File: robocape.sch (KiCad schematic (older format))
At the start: 5 parts

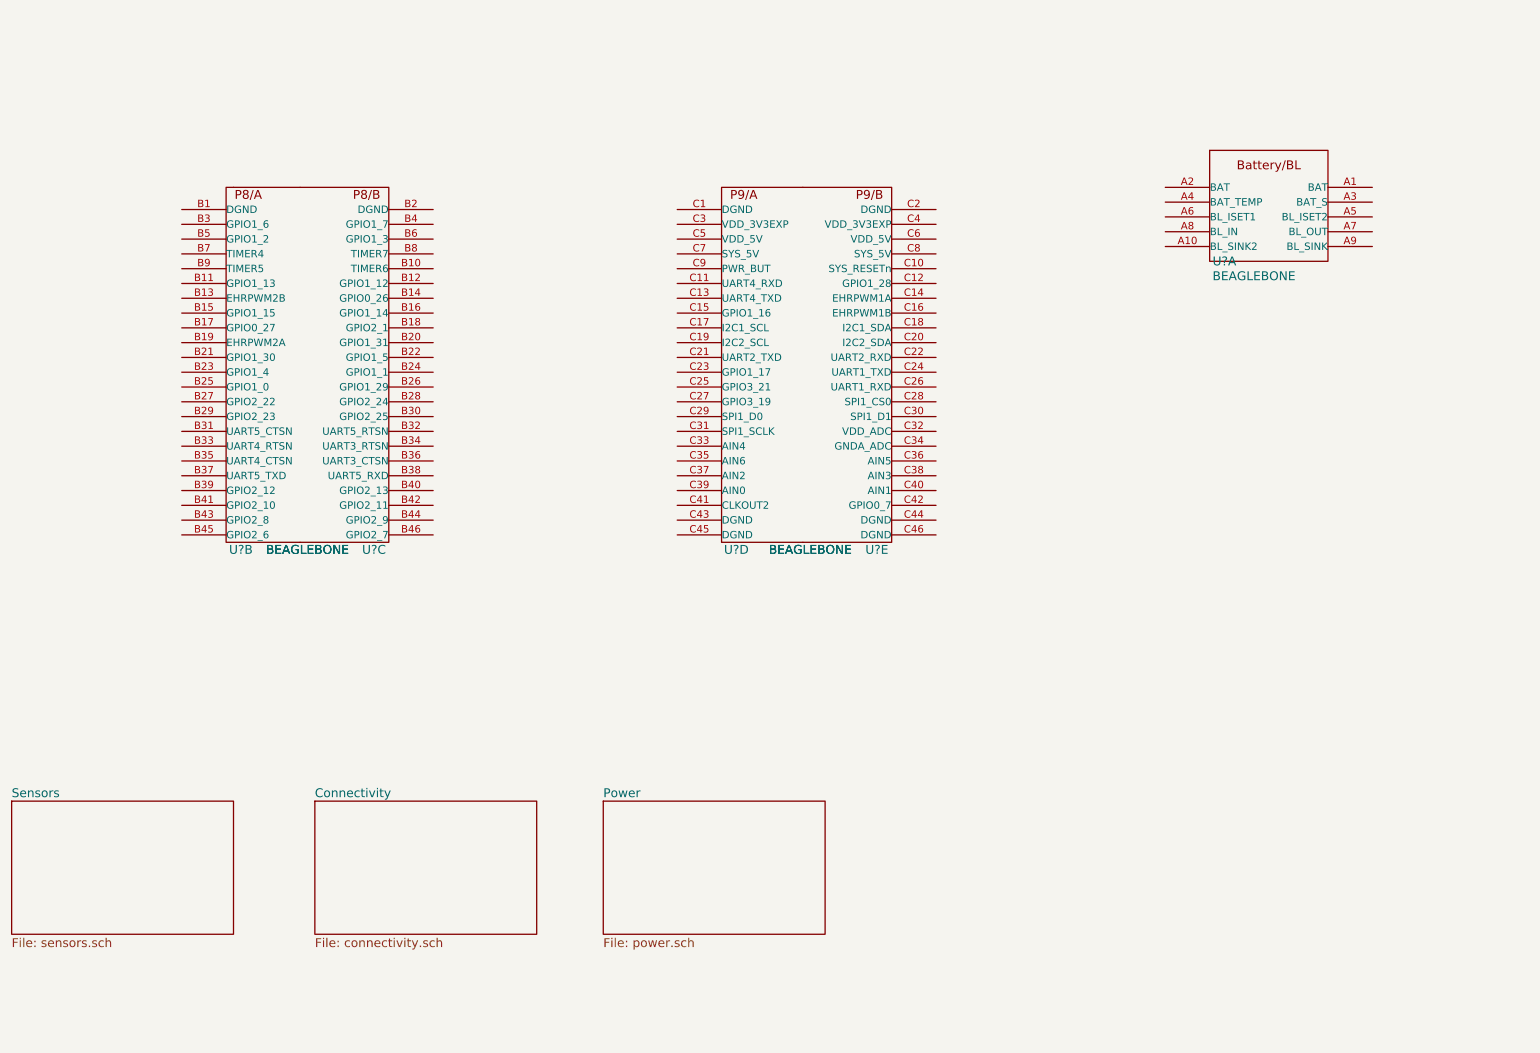
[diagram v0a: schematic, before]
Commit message: Schematic: EEPROM + IMU
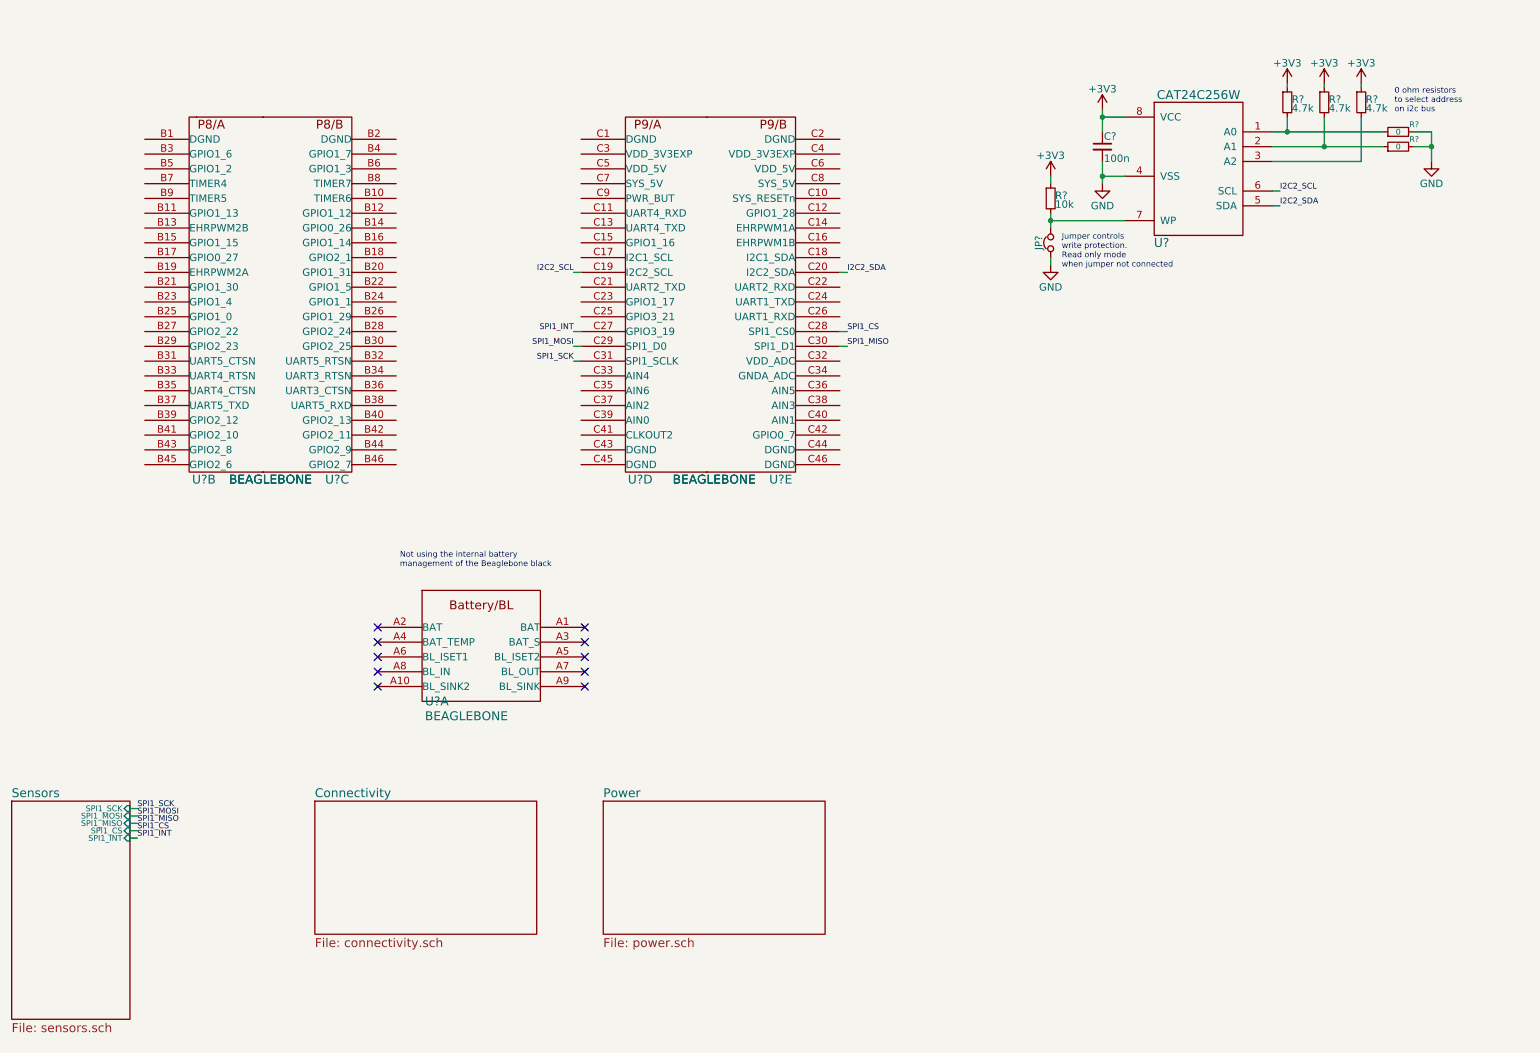
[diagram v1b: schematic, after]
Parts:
- added C?: 100n, symbol C_Small
- added JP?: Jumper_NC_Small, symbol Jumper_NC_Small
- added R?: 10k, symbol R_Small
- added R? (x3): 4.7k, symbol R_Small
- added R? (x2): 0, symbol R_Small
- added U?: CAT24C256W, symbol CAT24C256W
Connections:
- net I2C2_SCL: now reaches U?.C19 (I2C2_SCL)
- net I2C2_SCL: now also U?.6 (SCL)
- net SPI1_INT: now reaches U?.C27 (GPIO3_19)
- net SPI1_MOSI: now reaches U?.C29 (SPI1_D0)
- net SPI1_SCK: now reaches U?.C31 (SPI1_SCLK)
- net I2C2_SDA: now reaches U?.C20 (I2C2_SDA)
- net I2C2_SDA: now also U?.5 (SDA)
- net SPI1_CS: now reaches U?.C28 (SPI1_CS0)
- net SPI1_MISO: now reaches U?.C30 (SPI1_D1)
- new net: R?.1, R?.2, U?.1 (A0)
- new net: R?.1, R?.2, U?.2 (A1)
- new net: R?.2, U?.3 (A2)
- new net: JP?.2, R?.2, U?.7 (WP)
- new net +3V3: C?.1, R?.1, R?.1, R?.1, R?.1, U?.8 (VCC)
- new net GND: C?.2, JP?.1, R?.2, R?.2, U?.4 (VSS)
- no-connect marks 0 -> 10
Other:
- note added: "0 ohm resistors \nto select address\non i2c bus"
- note added: "Jumper controls\nwrite protection.\nRead only mode \nwhen jumper not connected"
- note added: "Not using the internal battery\nmanagement of the Beaglebone black"
- moved on the sheet: U?A, U?B, U?C, U?D, U?E

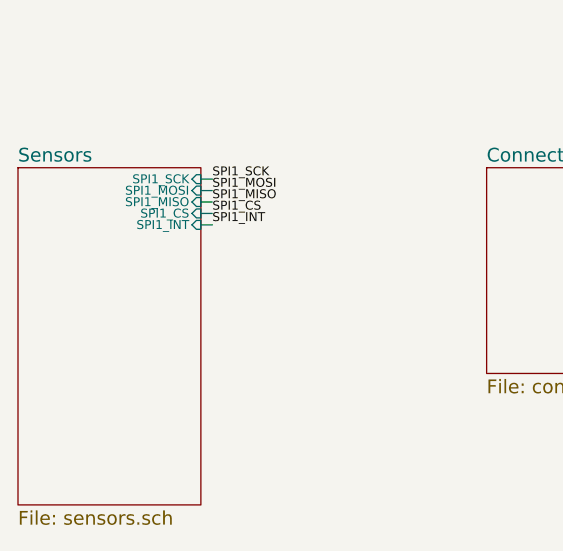
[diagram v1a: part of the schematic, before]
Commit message: Schematic: Barometer
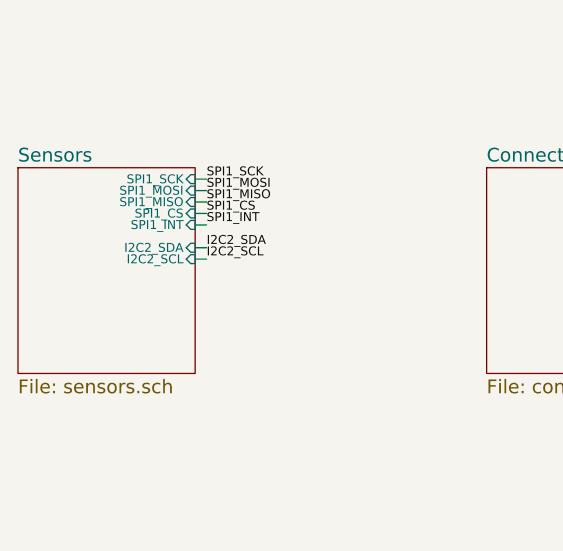
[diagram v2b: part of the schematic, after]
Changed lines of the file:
@@
 $EndComp
-$Sheet
-S 900  6050 800  1475
-U 55A505C3
-F0 "Sensors" 60
-F1 "sensors.sch" 60
-F2 "SPI1_SCK" I R 1700 6100 39
-F3 "SPI1_MOSI" I R 1700 6150 39
-F4 "SPI1_MISO" I R 1700 6200 39
-F5 "SPI1_CS" I R 1700 6250 39
-F6 "SPI1_INT" I R 1700 6300 39
-$EndSheet
 $Sheet
 S 2950 6050 1500 900
@@
 Text Notes 8000 2450 0    39   ~ 0
 Jumper controls\nwrite protection.\nRead only mode \nwhen jumper not connected
-Text Label 1750 6100 0    39   ~ 0
+Text Label 1725 6100 0    39   ~ 0
 SPI1_SCK
 Wire Wire Line
-	1750 6100 1700 6100
-Text Label 1750 6150 0    39   ~ 0
+	1725 6100 1675 6100
+Text Label 1725 6150 0    39   ~ 0
 SPI1_MOSI
-Text Label 1750 6200 0    39   ~ 0
+Text Label 1725 6200 0    39   ~ 0
 SPI1_MISO
-Text Label 1750 6250 0    39   ~ 0
+Text Label 1725 6250 0    39   ~ 0
 SPI1_CS
-Text Label 1750 6300 0    39   ~ 0
+Text Label 1725 6300 0    39   ~ 0
 SPI1_INT
 Wire Wire Line
-	1750 6150 1700 6150
-Wire Wire Line
-	1750 6200 1700 6200
-Wire Wire Line
-	1700 6250 1750 6250
-Wire Wire Line
-	1750 6300 1700 6300
+	1725 6150 1675 6150
+Wire Wire Line
+	1725 6200 1675 6200
+Wire Wire Line
+	1675 6250 1725 6250
+Wire Wire Line
+	1725 6300 1675 6300
 Text Label 4700 3075 2    39   ~ 0
 SPI1_SCK
@@
 Wire Wire Line
 	4700 2875 4750 2875
+$Sheet
+S 900  6050 775  900
+U 55A505C3
+F0 "Sensors" 60
+F1 "sensors.sch" 60
+F2 "SPI1_SCK" I R 1675 6100 39
+F3 "SPI1_MOSI" I R 1675 6150 39
+F4 "SPI1_MISO" I R 1675 6200 39
+F5 "SPI1_CS" I R 1675 6250 39
+F6 "SPI1_INT" I R 1675 6300 39
+F7 "I2C2_SDA" I R 1675 6400 39
+F8 "I2C2_SCL" I R 1675 6450 39
+$EndSheet
+Text Label 1725 6400 0    39   ~ 0
+I2C2_SDA
+Wire Wire Line
+	1725 6400 1675 6400
+Text Label 1725 6450 0    39   ~ 0
+I2C2_SCL
+Wire Wire Line
+	1725 6450 1675 6450
 $EndSCHEMATC

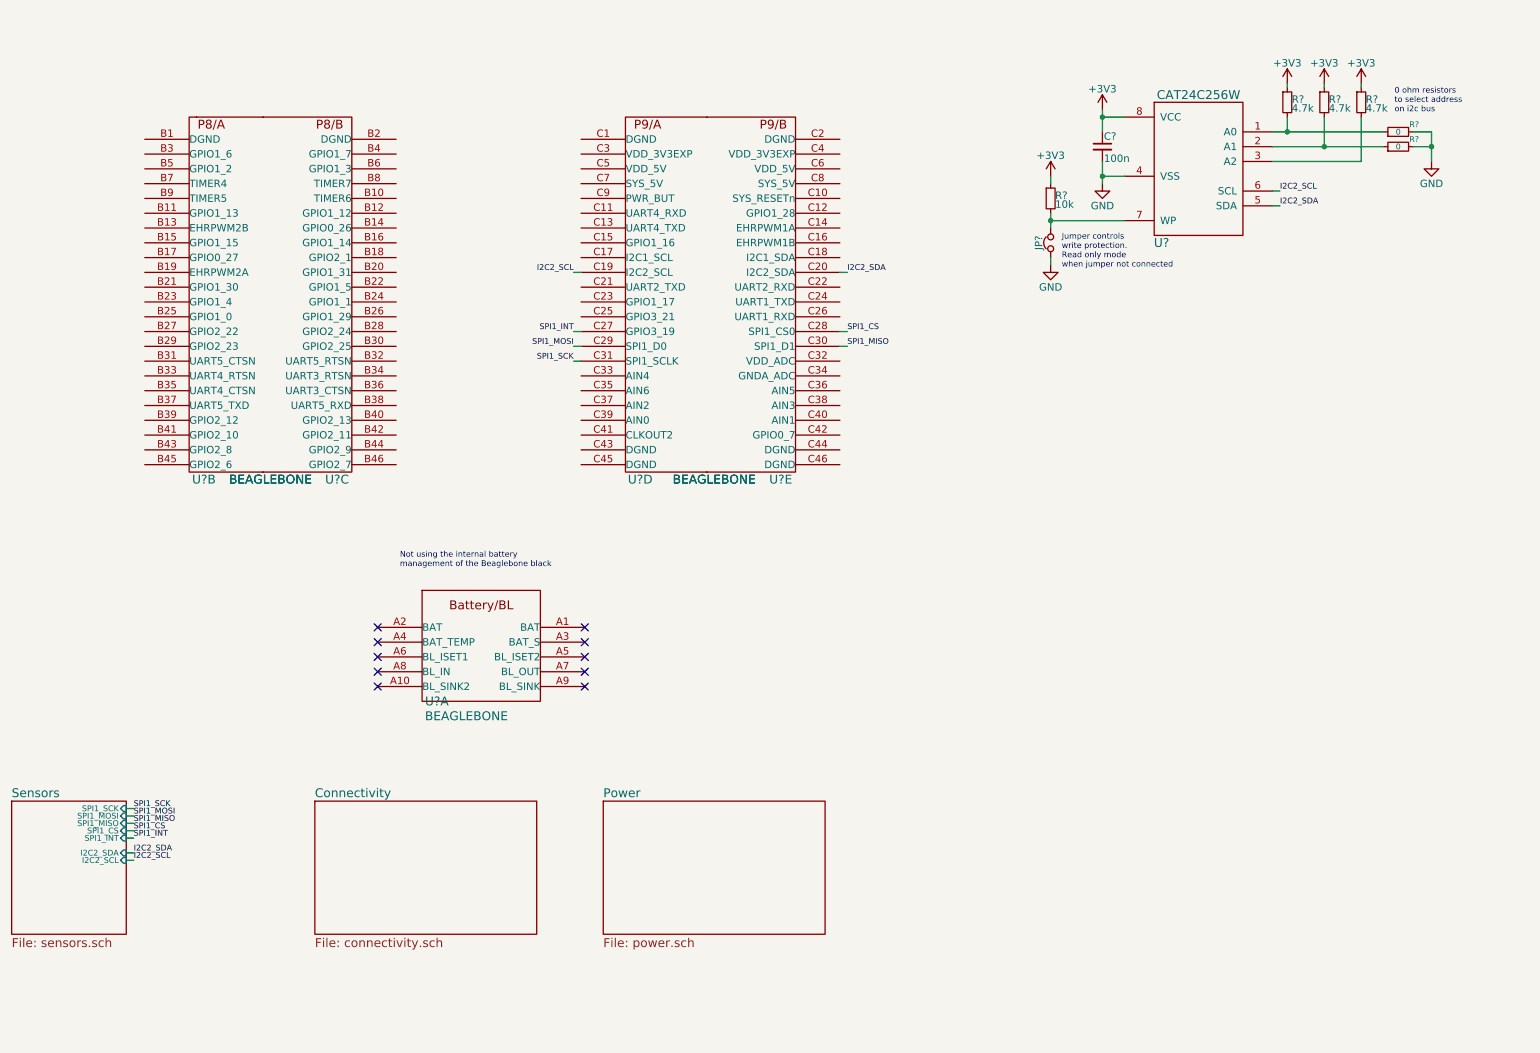
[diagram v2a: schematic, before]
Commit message: Schematic: Xbee header
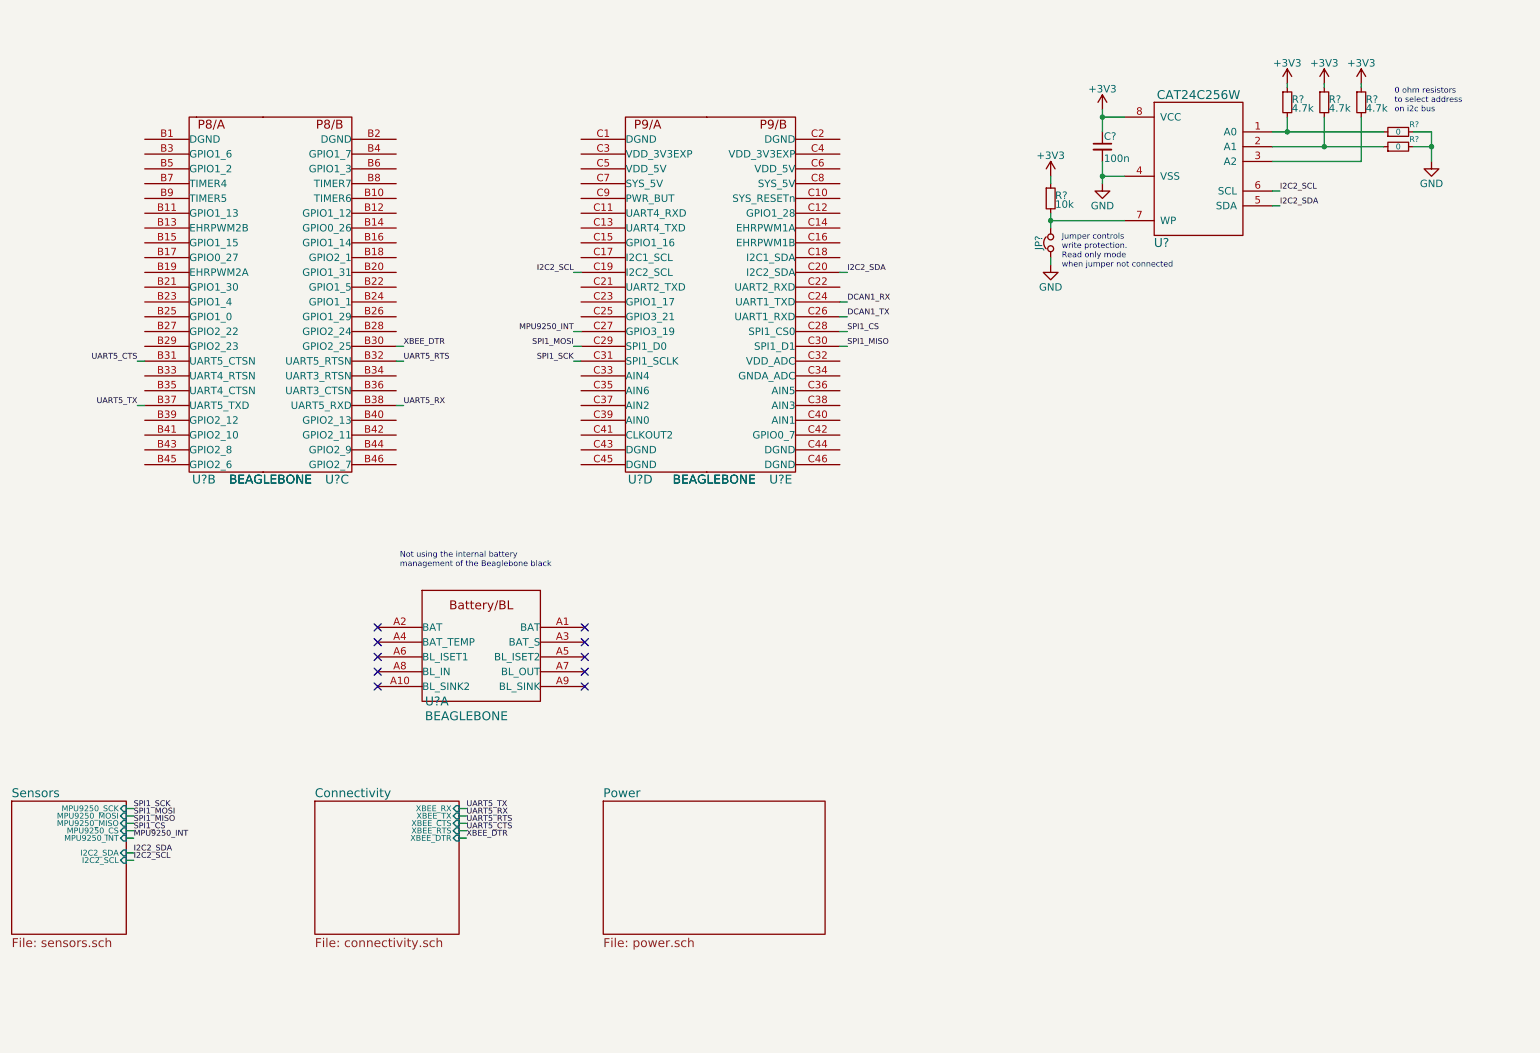
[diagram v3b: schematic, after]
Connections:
- net UART5_CTS: now reaches U?.B31 (UART5_CTSN)
- net UART5_TX: now reaches U?.B37 (UART5_TXD)
- net XBEE_DTR: now reaches U?.B30 (GPIO2_25)
- net UART5_RTS: now reaches U?.B32 (UART5_RTSN)
- net UART5_RX: now reaches U?.B38 (UART5_RXD)
- net DCAN1_RX: now reaches U?.C24 (UART1_TXD)
- net DCAN1_TX: now reaches U?.C26 (UART1_RXD)
- net SPI1_INT renamed MPU9250_INT
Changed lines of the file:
@@
 $EndComp
 $Sheet
-S 2950 6050 1500 900
+S 2950 6050 975  900
 U 55A505CD
 F0 "Connectivity" 60
 F1 "connectivity.sch" 60
+F2 "XBEE_RX" I R 3925 6100 39
+F3 "XBEE_TX" I R 3925 6150 39
+F4 "XBEE_CTS" I R 3925 6200 39
+F5 "XBEE_RTS" I R 3925 6250 39
+F6 "XBEE_DTR" I R 3925 6300 39
 $EndSheet
 $Sheet
@@
 SPI1_CS
 Text Label 1725 6300 0    39   ~ 0
-SPI1_INT
+MPU9250_INT
 Wire Wire Line
 	1725 6150 1675 6150
@@
 SPI1_CS
 Text Label 4700 2875 2    39   ~ 0
-SPI1_INT
+MPU9250_INT
 Wire Wire Line
 	6550 2875 6500 2875
@@
 Wire Wire Line
 	4700 3075 4750 3075
-Wire Wire Line
-	4700 2875 4750 2875
 $Sheet
 S 900  6050 775  900
@@
 F0 "Sensors" 60
 F1 "sensors.sch" 60
-F2 "SPI1_SCK" I R 1675 6100 39
-F3 "SPI1_MOSI" I R 1675 6150 39
-F4 "SPI1_MISO" I R 1675 6200 39
-F5 "SPI1_CS" I R 1675 6250 39
-F6 "SPI1_INT" I R 1675 6300 39
-F7 "I2C2_SDA" I R 1675 6400 39
-F8 "I2C2_SCL" I R 1675 6450 39
+F2 "I2C2_SDA" I R 1675 6400 39
+F3 "I2C2_SCL" I R 1675 6450 39
+F4 "MPU9250_INT" I R 1675 6300 39
+F5 "MPU9250_SCK" I R 1675 6100 39
+F6 "MPU9250_MOSI" I R 1675 6150 39
+F7 "MPU9250_MISO" I R 1675 6200 39
+F8 "MPU9250_CS" I R 1675 6250 39
 $EndSheet
 Text Label 1725 6400 0    39   ~ 0
@@
 Wire Wire Line
 	1725 6450 1675 6450
+Text Label 6550 2675 0    39   ~ 0
+DCAN1_RX
+Text Label 6550 2775 0    39   ~ 0
+DCAN1_TX
+Wire Wire Line
+	6550 2775 6500 2775
+Wire Wire Line
+	6500 2675 6550 2675
+Text Label 3975 6100 0    39   ~ 0
+UART5_TX
+Text Label 3975 6150 0    39   ~ 0
+UART5_RX
+Text Label 3975 6200 0    39   ~ 0
+UART5_RTS
+Text Label 3975 6250 0    39   ~ 0
+UART5_CTS
+Wire Wire Line
+	3975 6100 3925 6100
+Wire Wire Line
+	3925 6150 3975 6150
+Wire Wire Line
+	3975 6200 3925 6200
+Wire Wire Line
+	3925 6250 3975 6250
+Text Label 3975 6300 0    39   ~ 0
+XBEE_DTR
+Wire Wire Line
+	3975 6300 3925 6300
+Text Label 1750 3375 2    39   ~ 0
+UART5_TX
+Wire Wire Line
+	1750 3375 1800 3375
+Text Label 3550 3375 0    39   ~ 0
+UART5_RX
+Wire Wire Line
+	3550 3375 3500 3375
+Text Label 3550 3075 0    39   ~ 0
+UART5_RTS
+Text Label 1750 3075 2    39   ~ 0
+UART5_CTS
+Wire Wire Line
+	3550 3075 3500 3075
+Wire Wire Line
+	1750 3075 1800 3075
+Text Label 3550 2975 0    39   ~ 0
+XBEE_DTR
+Wire Wire Line
+	3550 2975 3500 2975
+Wire Wire Line
+	4700 2875 4750 2875
 $EndSCHEMATC
